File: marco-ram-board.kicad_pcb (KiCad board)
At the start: 4 copper layers, 160 x 100 mm, 183 parts, among them J201 PRG_USB, J202 MCU_RST, J203 MCU_BOOT0, J204 FT_TXD, J205 FT_RXD, J206 CONN_JTAG, J301 CONN_MCU_SERIAL, J302 EXT_CONN, J501 MCU_USB, J502 SD_Card, J503 CONN_DISP, J504 RJ45_Amphenol_RJMG1BD3B8K1ANR, J601 CONN_12V, J602 Screw_Terminal_01x02, Q201 MMBT3906, Q601 DMP3037LSS, SW301 SW_RST, SW302 SW_BOOT0, SW501 BTN0, SW502 BTN1, SW503 BTN2, SW504 BTN3, SW601 PWR_SW, U201 FT2232HL, U301 STM32F765IITx, U401 IS42S86400D, U402 IS42S86400D, U403 IS42S86400D, U404 IS42S86400D, U405 IS42S86400D, U406 IS42S86400D, U407 IS42S86400D, U408 IS42S86400D, U501 KSZ8081RNA, U601 LM2576S-3.3, Y201 12MHz, Y301 25MHz

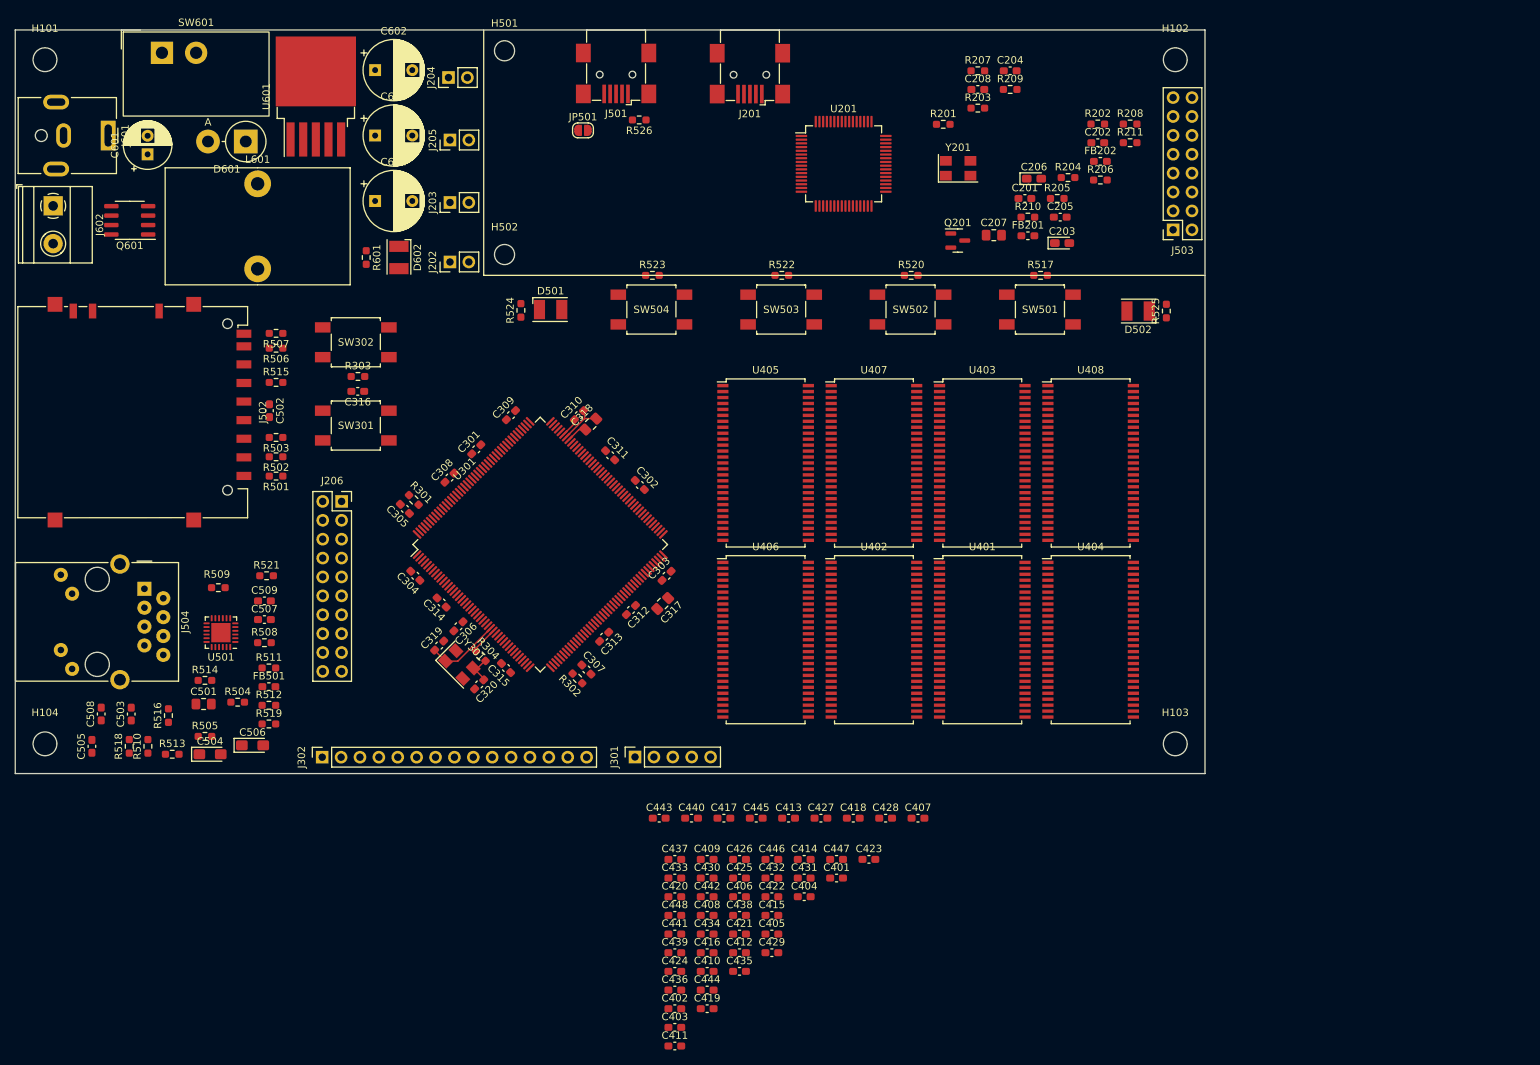
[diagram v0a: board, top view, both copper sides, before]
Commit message: Fix several footprints, adjust pcb layout.
- Change footprint for power switch, add the switch's datasheet.
- Rearrange power supply area of PCB to make new switch fit.
- Fix SD card socket footprint to be compatible with the schematic symbol. Add its datasheet
- Add pullups for SD card socket WP and CD (fixed footprint hardwires one side of the switches to GND)
- Add datasheet for the barrel jack.
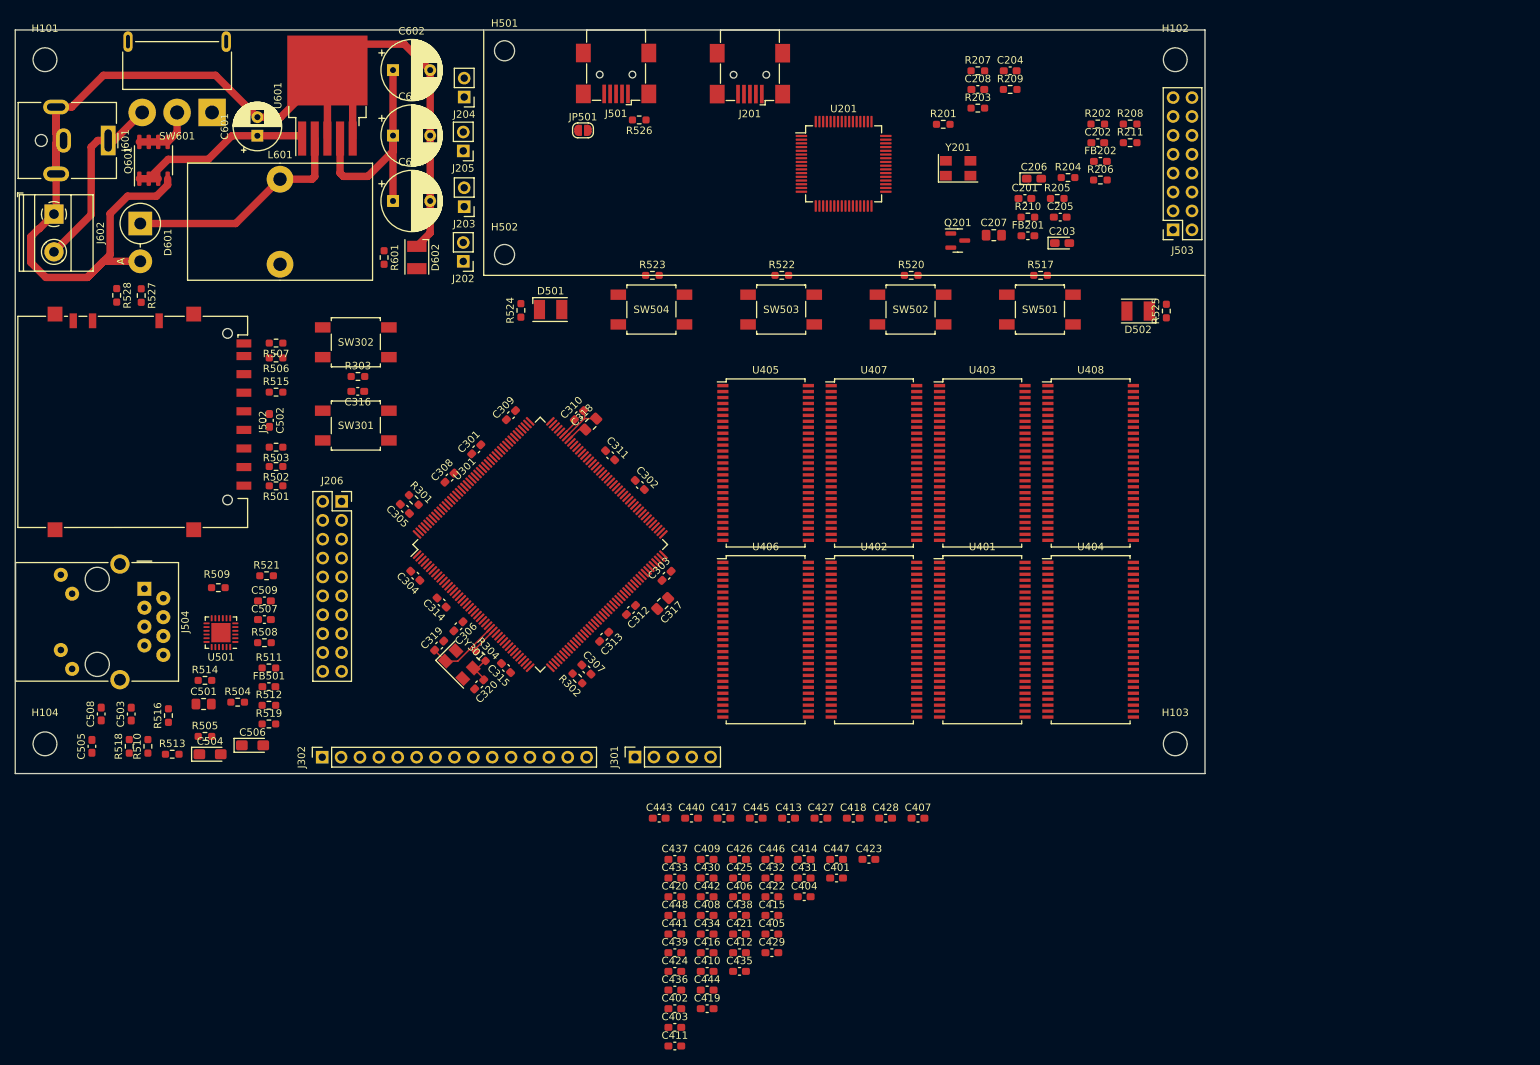
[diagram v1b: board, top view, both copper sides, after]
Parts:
- added R527: 47k, Resistor_SMD:R_0603_1608Metric_Pad0.98x0.95mm_HandSolder, F.Cu at (43.9, 59.7)
- added R528: 47k, Resistor_SMD:R_0603_1608Metric_Pad0.98x0.95mm_HandSolder, F.Cu at (40.6, 59.7)
- J502: footprint Connector_Card:SD_Hirose_DM1AA_SF_PEJ82 -> marco-ram-board:SD_Hirose_DM1AA_SF_PEJ82
- SW601: footprint marco-ram-board:SW_CuK_L101xxxMS02x_SPST_Straight -> marco-ram-board:SW_Slide_CuK_1101M2xxAxx2_SPDT_RightAngle
- moved D601 18.0 mm to (43.8, 50.0), turned to -90 degrees
- moved C601 15.0 mm to (59.6, 38.2)
- moved SW601 10.5 mm to (53.5, 35.1), turned to 180 degrees
- moved Q601 8.68 mm to (45.6, 41.5), turned to 90 degrees
- moved J204 3.37 mm to (87.4, 33.0), turned to 180 degrees
- moved L601 3.07 mm to (62.6, 44.1)
- moved D602 2.40 mm to (81.0, 54.6)
- moved C602 2.40 mm to (77.8, 29.4)
- moved C603 2.40 mm to (77.8, 38.2)
- moved C604 2.40 mm to (77.8, 47.0)
- moved R601 2.40 mm to (76.6, 54.6)
- moved J205 2.31 mm to (87.2, 40.3), turned to 180 degrees
- moved J203 2.00 mm to (87.4, 47.8), turned to 180 degrees
- moved J202 1.79 mm to (87.2, 55.1), turned to 180 degrees
- moved U601 1.56 mm to (69.0, 32.8)
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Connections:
- J601 pad 1: Net-(J601-Pad1) -> Net-(SW601-Pad3)
- J602 pad 2: Net-(J601-Pad1) -> Net-(SW601-Pad3)
- SW601 pad 1: Net-(J601-Pad1) -> unconnected-(SW601-Pad1)
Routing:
- net GND: track 6.03 -> 179.1 mm
- net VDD: track 2.60 -> 35.7 mm
- net Net-(D601-Pad1): track 0.00 -> 31.2 mm
- net Net-(C601-Pad1): track 0.00 -> 25.7 mm
- net Net-(SW601-Pad3): track 0.00 -> 25.0 mm
- net Net-(Q601-Pad5): track 0.00 -> 8.30 mm

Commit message: Fix overlapped label on DRAM data bus causing D16 and D18 nets to be connected together.
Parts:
- J601: value CONN_12V -> CONN_JACK_12V
- J602: value Screw_Terminal_01x02 -> CONN_SCREW_12V
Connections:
- U301 pad 87: /mcu/SDRAM.D16 -> /mcu/SDRAM.D18
- U403 pad 8: /mcu/SDRAM.D16 -> /mcu/SDRAM.D18
- U404 pad 8: /mcu/SDRAM.D16 -> /mcu/SDRAM.D18
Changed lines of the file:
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@@
   (net 238 "unconnected-(Y301-Pad2)")
   (net 239 "unconnected-(Y201-Pad4)")
-  (net 240 "Net-(SW601-Pad3)")
+  (net 240 "Net-(J601-Pad1)")
   (net 241 "unconnected-(SW601-Pad1)")
   (net 242 "/mcu/SDRAM.D16")
+  (net 243 "/mcu/SDRAM.D18")
   (footprint "Capacitor_THT:CP_Radial_D8.0mm_P5.00mm" (layer "F.Cu")
     (at 77.802047 47)
@@
       (effects (font (size 1 1) (thickness 0.15)))
     )
-    (fp_text value "CONN_12V" (at 0 13 90) (layer "F.Fab")
+    (fp_text value "CONN_JACK_12V" (at 0 13 90) (layer "F.Fab")
       (effects (font (size 1 1) (thickness 0.15)))
     )
@@
     (pad "" np_thru_hole circle (at 0 9 270) (size 1.6 1.6) (drill 1.6) (layers *.Cu *.Mask))
     (pad "1" thru_hole rect (at 0 0 270) (size 4 2) (drill oval 3 1) (layers *.Cu *.Mask)
-      (net 240 "Net-(SW601-Pad3)") (pintype "passive"))
+      (net 240 "Net-(J601-Pad1)") (pintype "passive"))
     (pad "2" thru_hole oval (at 0 6 270) (size 3.3 2) (drill oval 2.3 1) (layers *.Cu *.Mask)
       (net 1 "GND") (pintype "passive"))
@@
     (pad "7" smd rect (at -5.75 -5.6) (size 1.51 0.458) (layers "F.Cu" "F.Paste" "F.Mask"))
     (pad "8" smd rect (at -5.75 -4.8) (size 1.51 0.458) (layers "F.Cu" "F.Paste" "F.Mask")
-      (net 242 "/mcu/SDRAM.D16") (pinfunction "DQ2") (pintype "bidirectional"))
+      (net 243 "/mcu/SDRAM.D18") (pinfunction "DQ2") (pintype "bidirectional"))
     (pad "9" smd rect (at -5.75 -4) (size 1.51 0.458) (layers "F.Cu" "F.Paste" "F.Mask")
       (net 5 "VDD") (pinfunction "VDDQ") (pintype "power_in"))
@@
       (net 84 "Net-(Q601-Pad5)") (pinfunction "B") (pintype "passive"))
     (pad "3" thru_hole circle (at 9.398 0 180) (size 3.7084 3.7084) (drill 1.8542) (layers *.Cu *.Mask)
-      (net 240 "Net-(SW601-Pad3)") (pinfunction "C") (pintype "passive"))
+      (net 240 "Net-(J601-Pad1)") (pinfunction "C") (pintype "passive"))
     (model "${KICAD6_3DMODEL_DIR}/Button_Switch_THT.3dshapes/SW_CuK_JS202011CQN_DPDT_Straight.wrl"
       (offset (xyz -33.528 7.62 0))
@@
       (net 194 "/mcu/SDRAM.D17") (pinfunction "PH9") (pintype "bidirectional"))
     (pad "87" smd roundrect (at 10.25 12.675 45) (size 0.3 1.5) (layers "F.Cu" "F.Paste" "F.Mask") (roundrect_rratio 0.25)
-      (net 242 "/mcu/SDRAM.D16") (pinfunction "PH10") (pintype "bidirectional"))
+      (net 243 "/mcu/SDRAM.D18") (pinfunction "PH10") (pintype "bidirectional"))
     (pad "88" smd roundrect (at 10.75 12.675 45) (size 0.3 1.5) (layers "F.Cu" "F.Paste" "F.Mask") (roundrect_rratio 0.25)
       (net 195 "/mcu/SDRAM.D19") (pinfunction "PH11") (pintype "bidirectional"))
@@
       (effects (font (size 1 1) (thickness 0.15)))
     )
-    (fp_text value "Screw_Terminal_01x02" (at 2.54 5.66 90) (layer "F.Fab")
+    (fp_text value "CONN_SCREW_12V" (at 2.54 5.66 90) (layer "F.Fab")
       (effects (font (size 1 1) (thickness 0.15)))
     )
@@
       (net 1 "GND") (pinfunction "Pin_1") (pintype "passive"))
     (pad "2" thru_hole circle (at 5.08 0 270) (size 2.6 2.6) (drill 1.3) (layers *.Cu *.Mask)
-      (net 240 "Net-(SW601-Pad3)") (pinfunction "Pin_2") (pintype "passive"))
+      (net 240 "Net-(J601-Pad1)") (pinfunction "Pin_2") (pintype "passive"))
     (model "${KICAD6_3DMODEL_DIR}/TerminalBlock_Phoenix.3dshapes/TerminalBlock_Phoenix_MKDS-1,5-2-5.08_1x02_P5.08mm_Horizontal.wrl"
       (offset (xyz 0 0 0))
@@
     (pad "7" smd rect (at -5.75 -5.6) (size 1.51 0.458) (layers "F.Cu" "F.Paste" "F.Mask"))
     (pad "8" smd rect (at -5.75 -4.8) (size 1.51 0.458) (layers "F.Cu" "F.Paste" "F.Mask")
-      (net 242 "/mcu/SDRAM.D16") (pinfunction "DQ2") (pintype "bidirectional"))
+      (net 243 "/mcu/SDRAM.D18") (pinfunction "DQ2") (pintype "bidirectional"))
     (pad "9" smd rect (at -5.75 -4) (size 1.51 0.458) (layers "F.Cu" "F.Paste" "F.Mask")
       (net 5 "VDD") (pinfunction "VDDQ") (pintype "power_in"))

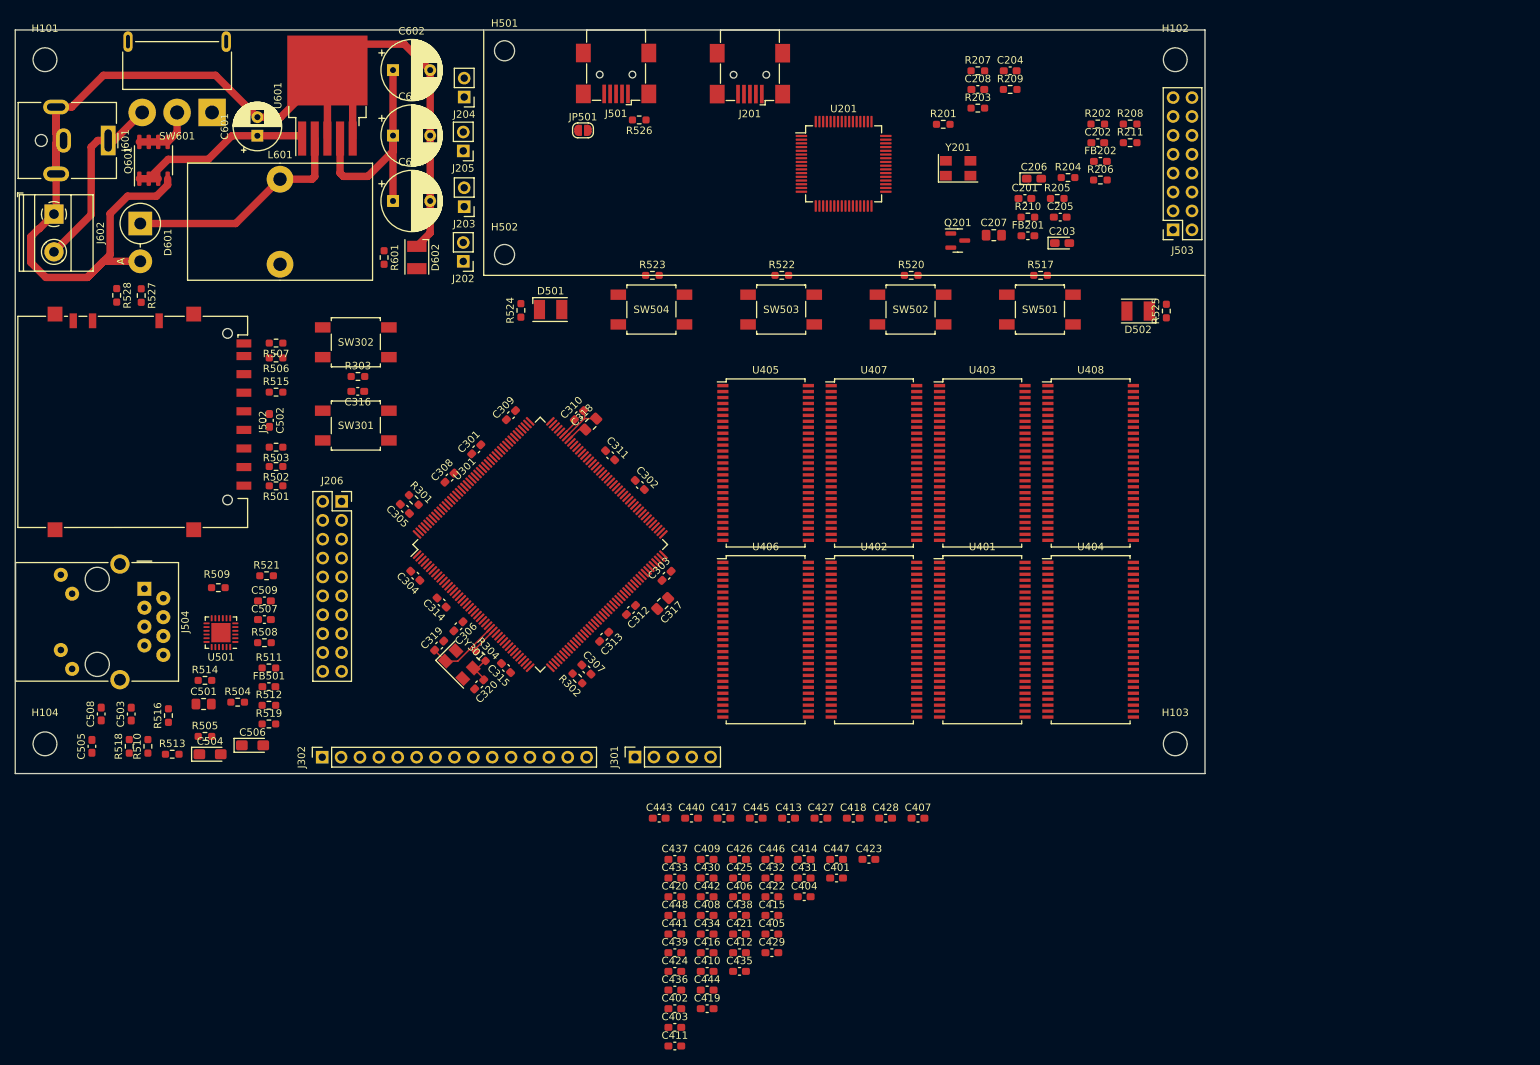
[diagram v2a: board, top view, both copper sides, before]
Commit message: Finish placement, start routing.
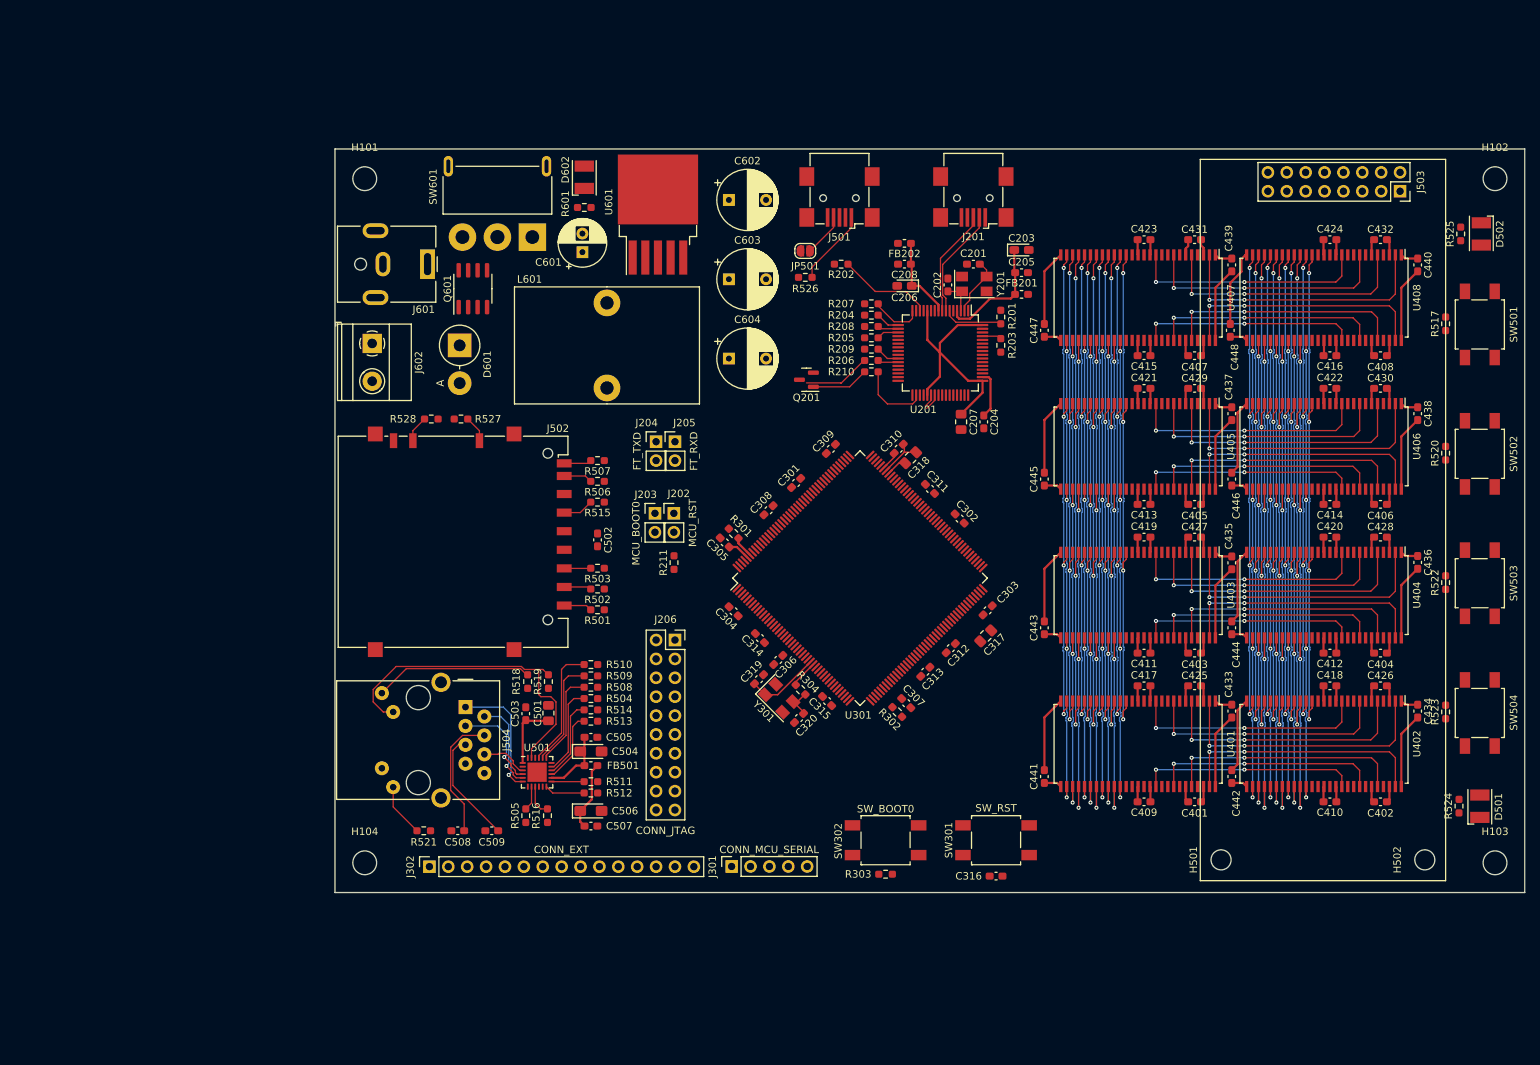
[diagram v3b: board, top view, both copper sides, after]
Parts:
- J302: value EXT_CONN -> CONN_EXT
- moved H502 148.1 mm to (216.6, 135.6), turned to 90 degrees
- moved H501 145.3 mm to (189.2, 135.6), turned to 90 degrees
- moved R524 142.7 mm to (221.2, 128.4)
- moved D501 141.7 mm to (224.0, 128.4), turned to 90 degrees
- moved C424 132.1 mm to (203.8, 52.2)
- moved SW504 123.9 mm to (224.0, 115.9), turned to 90 degrees
- moved C440 122.8 mm to (215.6, 55.6), turned to -90 degrees
- moved R523 121.8 mm to (219.4, 115.7), turned to 90 degrees
- moved C439 119.0 mm to (190.6, 55.6), turned to -90 degrees
- moved C432 118.6 mm to (210.6, 52.2), turned to 180 degrees
- moved C408 117.7 mm to (210.6, 67.8)
- moved C416 116.0 mm to (203.8, 67.8), turned to 180 degrees
- moved C436 115.3 mm to (215.6, 95.6), turned to -90 degrees
- moved C438 113.4 mm to (215.6, 75.6), turned to -90 degrees
- moved C430 112.0 mm to (210.6, 72.2), turned to 180 degrees
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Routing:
- net VDD: track 35.7 -> 189.9 mm
- net /mcu/SDRAM.~{RAS}: track 0.00 -> 147.5 mm, vias 0 -> 8
- net /mcu/SDRAM.BA1: track 0.00 -> 147.5 mm, vias 0 -> 8
- net /mcu/SDRAM.A1: track 0.00 -> 147.5 mm, vias 0 -> 8
- net /mcu/SDRAM.A9: track 0.00 -> 143.8 mm, vias 0 -> 8
- net /mcu/SDRAM.A6: track 0.00 -> 143.8 mm, vias 0 -> 8
- net /mcu/SDRAM.A10: track 0.00 -> 141.9 mm, vias 0 -> 8
- net /mcu/SDRAM.A2: track 0.00 -> 141.9 mm, vias 0 -> 8
- net /mcu/SDRAM.~{WE}: track 0.00 -> 141.4 mm, vias 0 -> 8
- net /mcu/SDRAM.A5: track 0.00 -> 138.2 mm, vias 0 -> 8
- net /mcu/SDRAM.A12: track 0.00 -> 138.2 mm, vias 0 -> 8
- net /mcu/SDRAM.A8: track 0.00 -> 138.2 mm, vias 0 -> 8
- net /mcu/SDRAM.~{CAS}: track 0.00 -> 136.3 mm, vias 0 -> 8
- net /mcu/SDRAM.BA0: track 0.00 -> 136.3 mm, vias 0 -> 8
- net /mcu/SDRAM.A0: track 0.00 -> 136.3 mm, vias 0 -> 8
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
